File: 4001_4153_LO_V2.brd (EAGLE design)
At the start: 109 x 63 mm, 112 parts, among them IC1 74LVC2G17GV,125, IC10 MCP6H01, IC2 74LVC2G17GV,125, IC3 74LVC2G17GV,125, IC4 ADF4001BRUZ, IC5 ATTINY45V-10SU, IC6 7805DT, IC7 7809DT, IC8 LD1117AS33TR, IC9 ADF4153BRUZ-RL7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

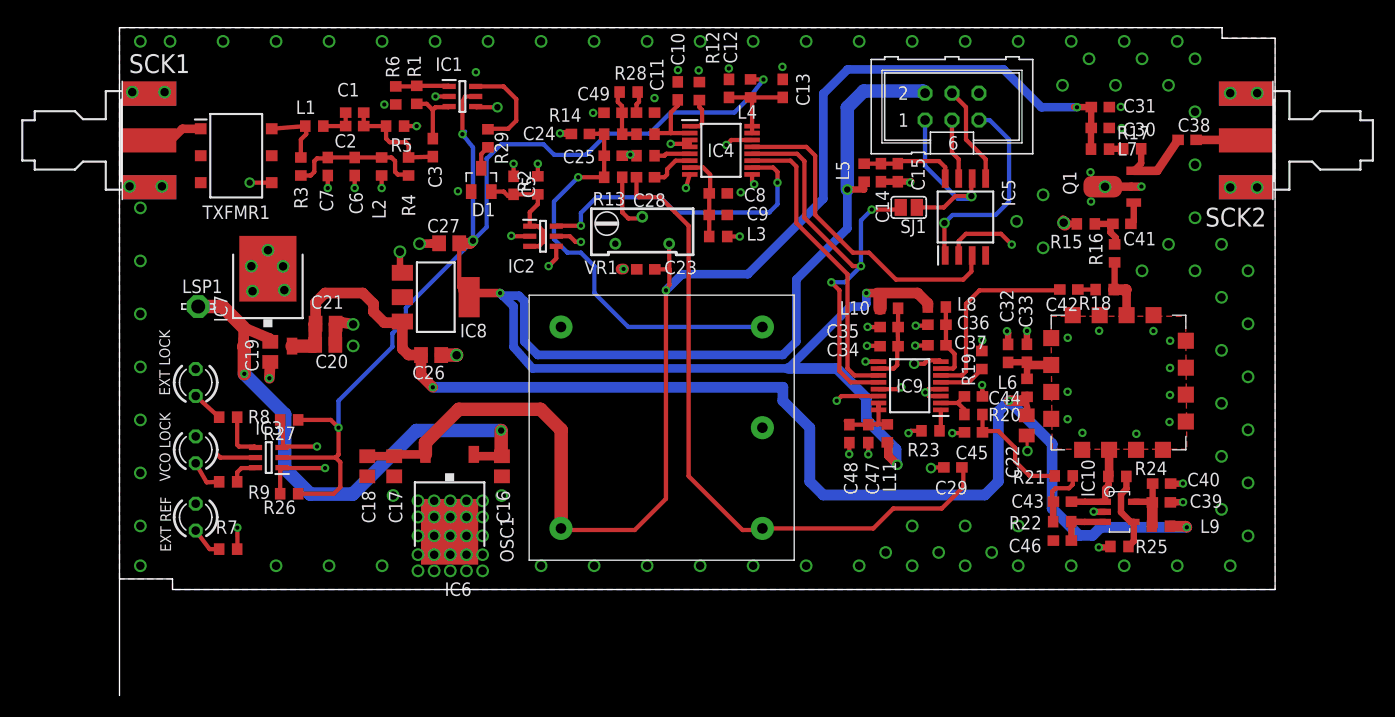
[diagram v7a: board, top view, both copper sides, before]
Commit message: Tracking corrections
Minor clearance issues
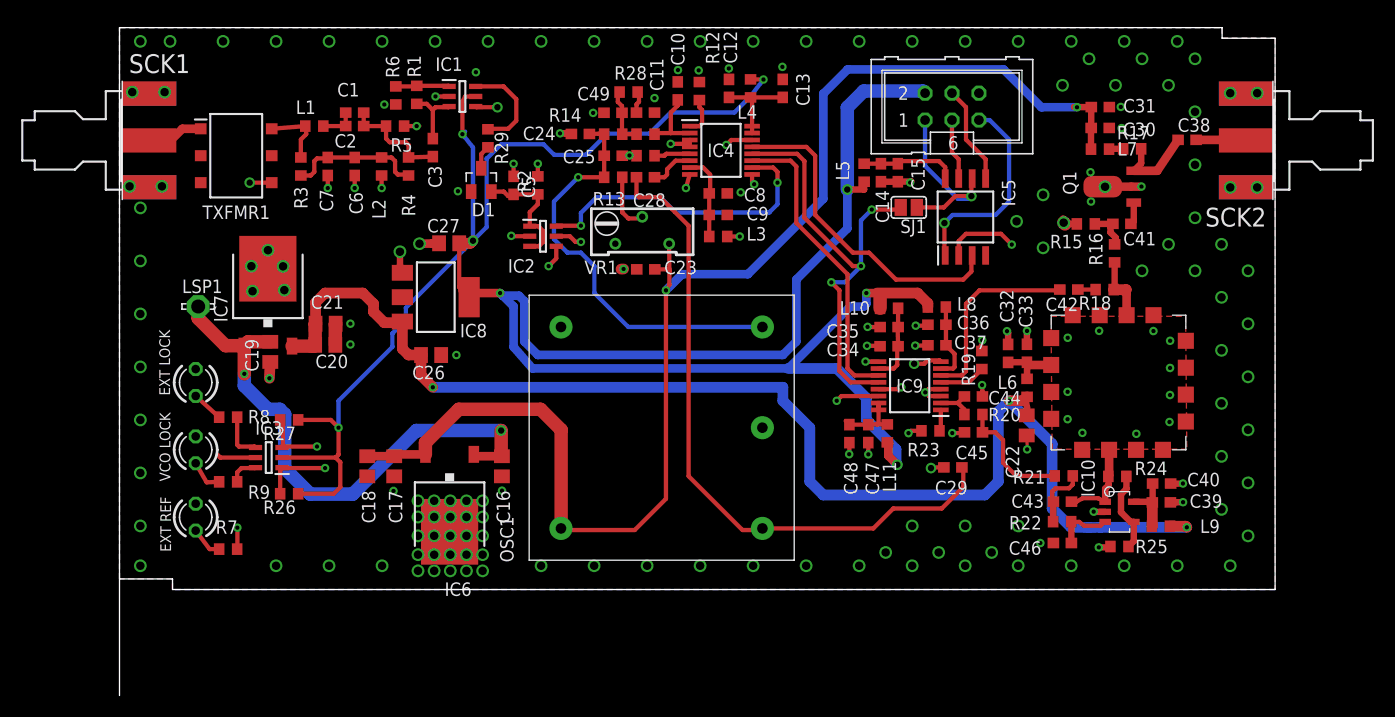
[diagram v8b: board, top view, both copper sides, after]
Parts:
- moved C46 0.23 mm to (88.9, 4.39)
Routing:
- net GND: track 61.8 -> 59.0 mm, vias 187 -> 188
- net +9V: track 125.6 -> 125.0 mm
- net LOOP_IN: track 11.0 -> 11.6 mm
